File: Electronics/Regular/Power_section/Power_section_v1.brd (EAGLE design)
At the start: 33 x 47 mm, 14 parts

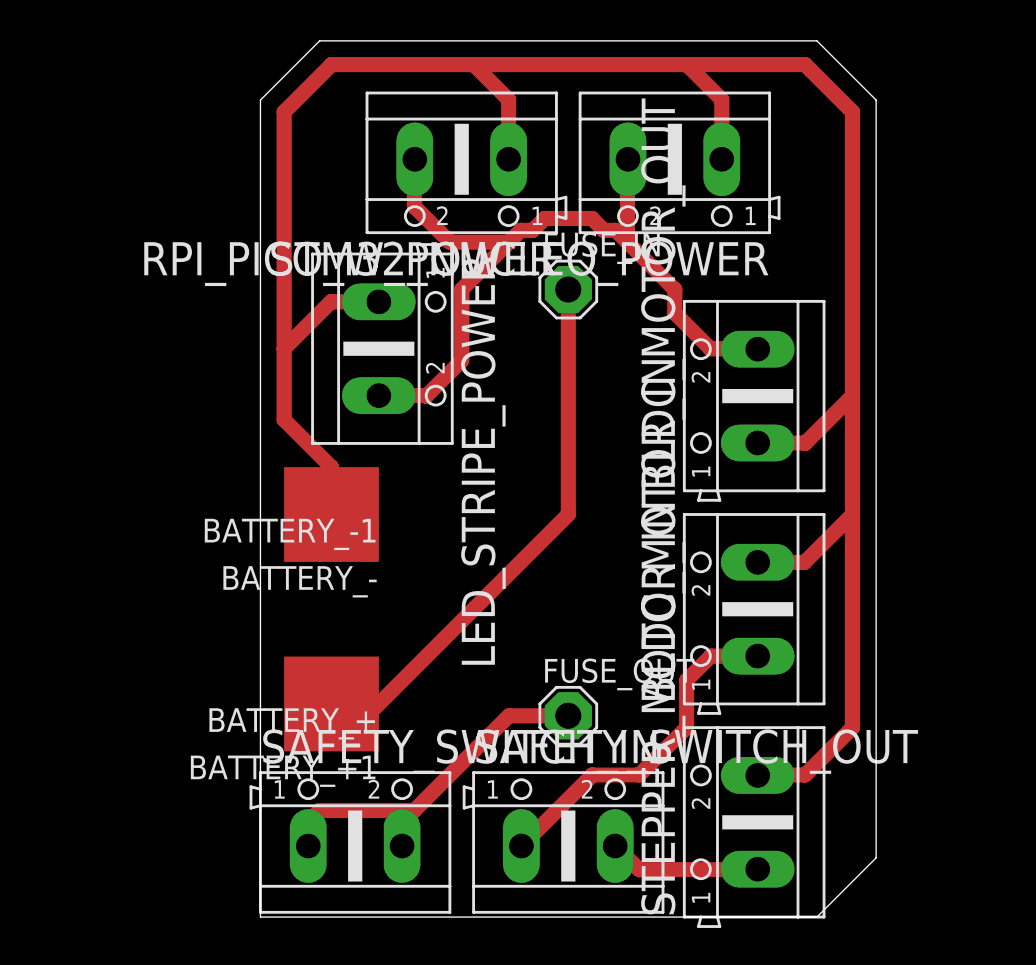
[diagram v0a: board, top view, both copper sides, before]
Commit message: Power section improved
What has been improved:
- changed fuse holder slot for the smaller model,
- made wires wider
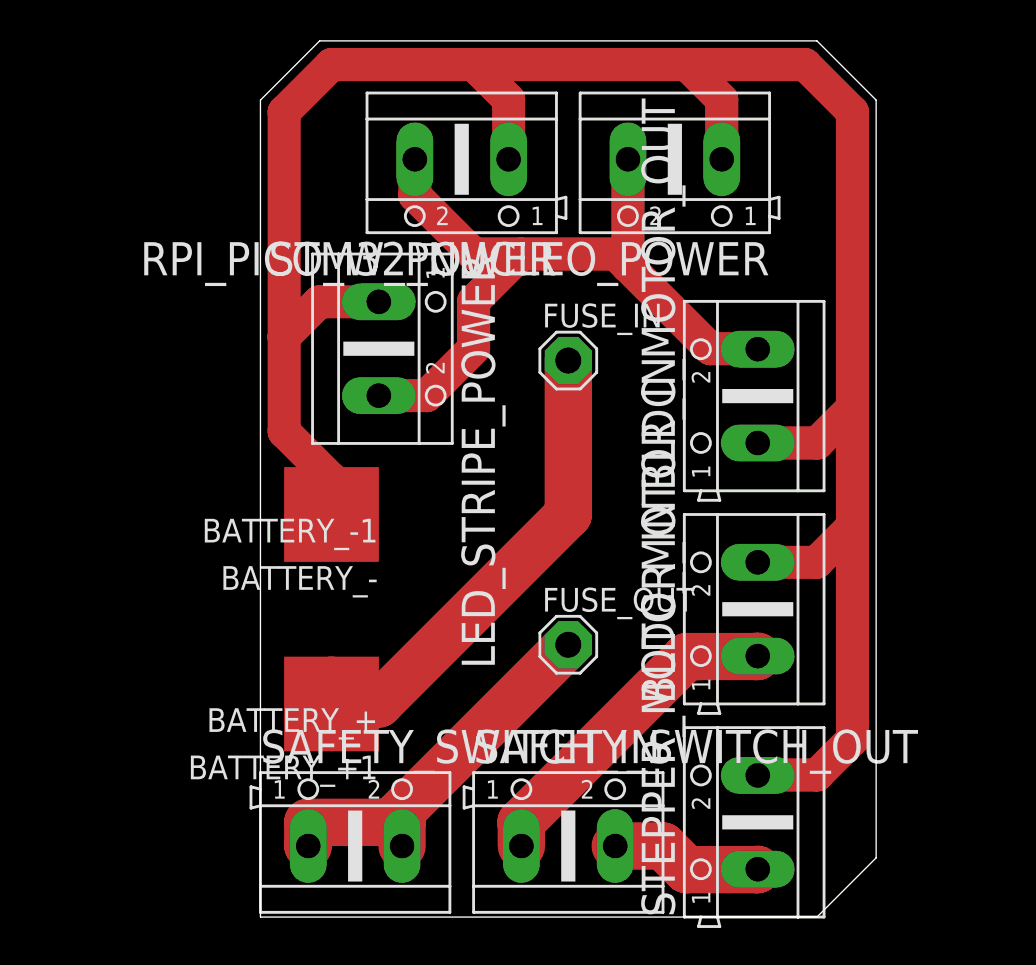
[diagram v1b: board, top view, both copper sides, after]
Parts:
- moved FUSE_IN 3.81 mm to (16.5, 29.8)
- moved FUSE_OUT 3.81 mm to (16.5, 14.6)
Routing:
- net N$1: track 32.0 -> 28.2 mm
- net 5V: track 43.0 -> 41.7 mm
- net 12V: track 19.8 -> 20.9 mm
- net BLDC_MOTOR: track 18.4 -> 17.7 mm

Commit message: Power section improved
What has been improved:
- moved BAT+ and BAT- pads to the very left,
- made wires wider
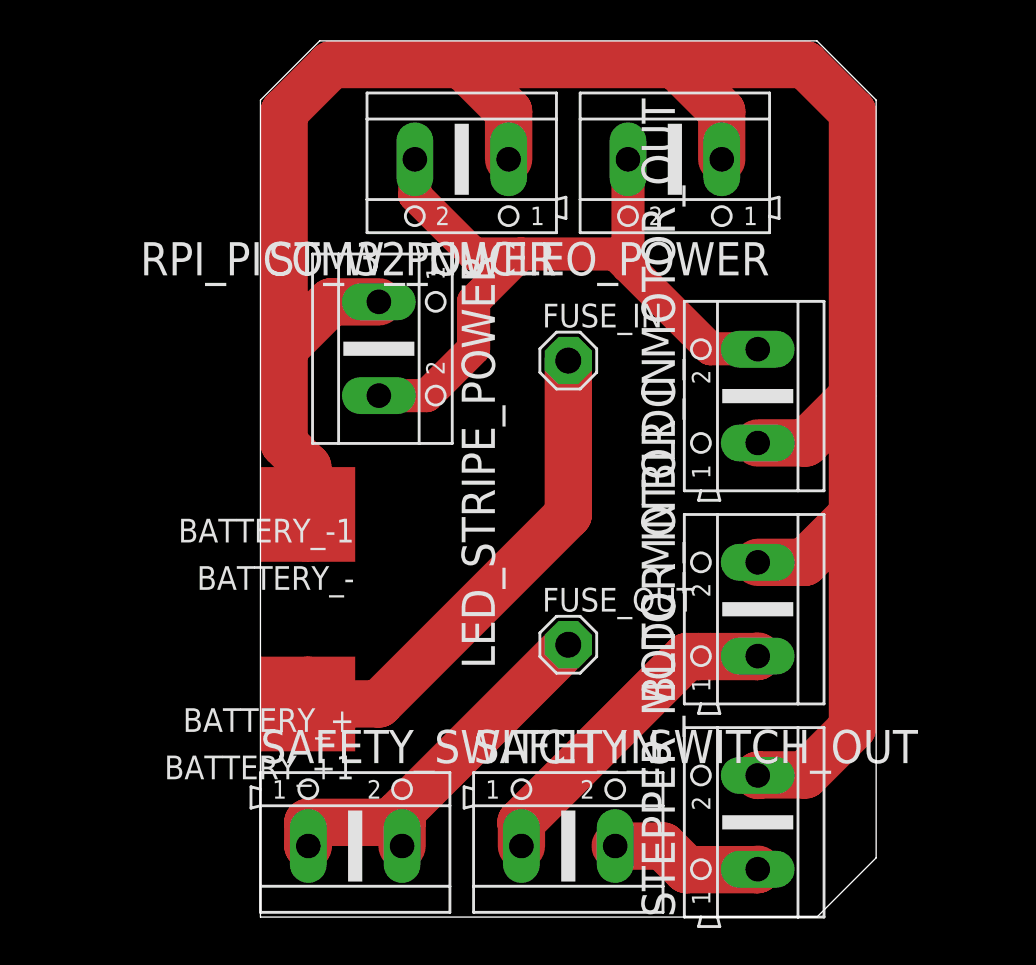
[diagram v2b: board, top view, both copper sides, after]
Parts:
- moved BATTERY_+ 1.27 mm to (2.54, 12.7)
- moved BATTERY_+1 1.27 mm to (2.54, 10.2)
- moved BATTERY_- 1.27 mm to (2.54, 20.3)
- moved BATTERY_-1 1.27 mm to (2.54, 22.9)
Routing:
- net N$1: track 28.2 -> 29.5 mm
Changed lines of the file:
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@@
 </autorouter>
 <elements>
-<element name="BATTERY_-" library="wirepad" package="SMD2,54-5,08" value="WIREPADSMD2,54-5,08" x="3.81" y="20.32" rot="R90"/>
-<element name="BATTERY_+" library="wirepad" package="SMD2,54-5,08" value="WIREPADSMD2,54-5,08" x="3.81" y="12.7" rot="R90"/>
+<element name="BATTERY_-" library="wirepad" package="SMD2,54-5,08" value="WIREPADSMD2,54-5,08" x="2.54" y="20.32" rot="R90"/>
+<element name="BATTERY_+" library="wirepad" package="SMD2,54-5,08" value="WIREPADSMD2,54-5,08" x="2.54" y="12.7" rot="R90"/>
 <element name="SAFETY_SWITCH_IN" library="con-ptr500" package="AK500/2" value="" x="5.08" y="3.81">
 <attribute name="OC_FARNELL" value="unknown" x="5.08" y="3.81" size="1.778" layer="27" display="off"/>
@@
 <attribute name="MPN" value="" x="21.59" y="41.91" size="1.778" layer="27" rot="R270" display="off"/>
 </element>
-<element name="BATTERY_-1" library="wirepad" package="SMD2,54-5,08" value="WIREPADSMD2,54-5,08" x="3.81" y="22.86" rot="R90"/>
-<element name="BATTERY_+1" library="wirepad" package="SMD2,54-5,08" value="WIREPADSMD2,54-5,08" x="3.81" y="10.16" rot="R90"/>
+<element name="BATTERY_-1" library="wirepad" package="SMD2,54-5,08" value="WIREPADSMD2,54-5,08" x="2.54" y="22.86" rot="R90"/>
+<element name="BATTERY_+1" library="wirepad" package="SMD2,54-5,08" value="WIREPADSMD2,54-5,08" x="2.54" y="10.16" rot="R90"/>
 <element name="FUSE_IN" library="solpad" package="SE14" value="SE14" x="16.51" y="29.845"/>
 <element name="FUSE_OUT" library="solpad" package="SE14" value="SE14" x="16.51" y="14.605"/>
@@
 <contactref element="BLDC_MOTOR_OUT" pad="1"/>
 <contactref element="BATTERY_-1" pad="1"/>
-<wire x1="3.81" y1="20.32" x2="3.81" y2="22.86" width="1.27" layer="1"/>
-<wire x1="3.81" y1="22.86" x2="3.81" y2="23.495" width="1.778" layer="1"/>
-<wire x1="3.81" y1="23.495" x2="1.27" y2="26.035" width="1.778" layer="1"/>
-<wire x1="1.27" y1="26.035" x2="1.27" y2="31.115" width="1.778" layer="1"/>
-<wire x1="1.27" y1="31.115" x2="1.27" y2="43.18" width="1.778" layer="1"/>
-<wire x1="1.27" y1="43.18" x2="3.81" y2="45.72" width="1.778" layer="1"/>
-<wire x1="3.81" y1="45.72" x2="11.43" y2="45.72" width="1.778" layer="1"/>
-<wire x1="11.43" y1="45.72" x2="22.86" y2="45.72" width="1.778" layer="1"/>
-<wire x1="22.86" y1="45.72" x2="29.21" y2="45.72" width="1.778" layer="1"/>
-<wire x1="29.21" y1="45.72" x2="31.75" y2="43.18" width="1.778" layer="1"/>
-<wire x1="31.75" y1="43.18" x2="31.75" y2="27.305" width="1.778" layer="1"/>
-<wire x1="31.75" y1="27.305" x2="31.75" y2="20.955" width="1.778" layer="1"/>
-<wire x1="31.75" y1="20.955" x2="31.75" y2="9.525" width="1.778" layer="1"/>
-<wire x1="31.75" y1="9.525" x2="29.845" y2="7.62" width="1.778" layer="1"/>
-<wire x1="29.845" y1="7.62" x2="26.6954" y2="7.62" width="1.778" layer="1"/>
-<wire x1="26.6954" y1="7.62" x2="26.67" y2="7.5946" width="1.778" layer="1"/>
-<wire x1="26.67" y1="19.0246" x2="29.8196" y2="19.0246" width="1.778" layer="1"/>
-<wire x1="29.8196" y1="19.0246" x2="31.75" y2="20.955" width="1.778" layer="1"/>
-<wire x1="26.67" y1="25.4254" x2="29.8704" y2="25.4254" width="1.778" layer="1"/>
-<wire x1="29.8704" y1="25.4254" x2="31.75" y2="27.305" width="1.778" layer="1"/>
-<wire x1="13.3096" y1="40.64" x2="13.3096" y2="43.8404" width="1.778" layer="1"/>
-<wire x1="13.3096" y1="43.8404" x2="11.43" y2="45.72" width="1.778" layer="1"/>
-<wire x1="24.7396" y1="40.64" x2="24.7396" y2="43.8404" width="1.778" layer="1"/>
-<wire x1="24.7396" y1="43.8404" x2="22.86" y2="45.72" width="1.778" layer="1"/>
-<wire x1="6.35" y1="32.9946" x2="3.1496" y2="32.9946" width="1.778" layer="1"/>
-<wire x1="3.1496" y1="32.9946" x2="1.27" y2="31.115" width="1.778" layer="1"/>
+<wire x1="2.54" y1="20.32" x2="2.54" y2="22.86" width="2.54" layer="1"/>
+<wire x1="2.54" y1="22.86" x2="2.54" y2="24.13" width="2.54" layer="1"/>
+<wire x1="2.54" y1="24.13" x2="1.27" y2="25.4" width="2.54" layer="1"/>
+<wire x1="1.27" y1="25.4" x2="1.27" y2="30.48" width="2.54" layer="1"/>
+<wire x1="1.27" y1="30.48" x2="1.27" y2="43.18" width="2.54" layer="1"/>
+<wire x1="1.27" y1="43.18" x2="3.81" y2="45.72" width="2.54" layer="1"/>
+<wire x1="3.81" y1="45.72" x2="10.795" y2="45.72" width="2.54" layer="1"/>
+<wire x1="10.795" y1="45.72" x2="22.225" y2="45.72" width="2.54" layer="1"/>
+<wire x1="22.225" y1="45.72" x2="29.21" y2="45.72" width="2.54" layer="1"/>
+<wire x1="29.21" y1="45.72" x2="31.75" y2="43.18" width="2.54" layer="1"/>
+<wire x1="31.75" y1="43.18" x2="31.75" y2="27.94" width="2.54" layer="1"/>
+<wire x1="31.75" y1="27.94" x2="31.75" y2="21.59" width="2.54" layer="1"/>
+<wire x1="31.75" y1="21.59" x2="31.75" y2="10.16" width="2.54" layer="1"/>
+<wire x1="31.75" y1="10.16" x2="29.21" y2="7.62" width="2.54" layer="1"/>
+<wire x1="29.21" y1="7.62" x2="26.6954" y2="7.62" width="2.54" layer="1"/>
+<wire x1="26.6954" y1="7.62" x2="26.67" y2="7.5946" width="2.54" layer="1"/>
+<wire x1="26.67" y1="19.0246" x2="29.1846" y2="19.0246" width="2.54" layer="1"/>
+<wire x1="29.1846" y1="19.0246" x2="31.75" y2="21.59" width="2.54" layer="1"/>
+<wire x1="26.67" y1="25.4254" x2="29.2354" y2="25.4254" width="2.54" layer="1"/>
+<wire x1="29.2354" y1="25.4254" x2="31.75" y2="27.94" width="2.54" layer="1"/>
+<wire x1="24.7396" y1="40.64" x2="24.7396" y2="43.2054" width="2.54" layer="1"/>
+<wire x1="24.7396" y1="43.2054" x2="22.225" y2="45.72" width="2.54" layer="1"/>
+<wire x1="13.3096" y1="40.64" x2="13.3096" y2="43.2054" width="2.54" layer="1"/>
+<wire x1="13.3096" y1="43.2054" x2="10.795" y2="45.72" width="2.54" layer="1"/>
+<wire x1="6.35" y1="32.9946" x2="3.7846" y2="32.9946" width="2.54" layer="1"/>
+<wire x1="3.7846" y1="32.9946" x2="1.27" y2="30.48" width="2.54" layer="1"/>
 </signal>
 <signal name="STEPPER_MOTOR">
@@
 <contactref element="BATTERY_+1" pad="1"/>
 <contactref element="FUSE_IN" pad="MP"/>
-<wire x1="3.81" y1="12.7" x2="3.81" y2="10.16" width="2.54" layer="1"/>
-<wire x1="3.81" y1="12.7" x2="5.08" y2="11.43" width="2.54" layer="1"/>
-<wire x1="5.08" y1="11.43" x2="6.35" y2="11.43" width="2.54" layer="1"/>
 <wire x1="6.35" y1="11.43" x2="16.51" y2="21.59" width="2.54" layer="1"/>
 <wire x1="16.51" y1="21.59" x2="16.51" y2="29.845" width="2.54" layer="1"/>
+<wire x1="2.54" y1="10.16" x2="2.54" y2="12.7" width="2.54" layer="1"/>
+<wire x1="2.54" y1="12.7" x2="3.81" y2="11.43" width="2.54" layer="1"/>
+<wire x1="3.81" y1="11.43" x2="6.35" y2="11.43" width="2.54" layer="1"/>
 </signal>
 </signals>
